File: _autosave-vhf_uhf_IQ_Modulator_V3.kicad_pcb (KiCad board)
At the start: 2 copper layers, 71 parts, among them J1 CONN_01X03, J2 TEST_1P, J3 Audio-Jack-3, J4 CONN_01X04, J5 SMA Edge FM, Q1 BC817-40, Q2 BC817-40, Q3 BC817-40, U1 TRF3701, U2 MMZ09332BT1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

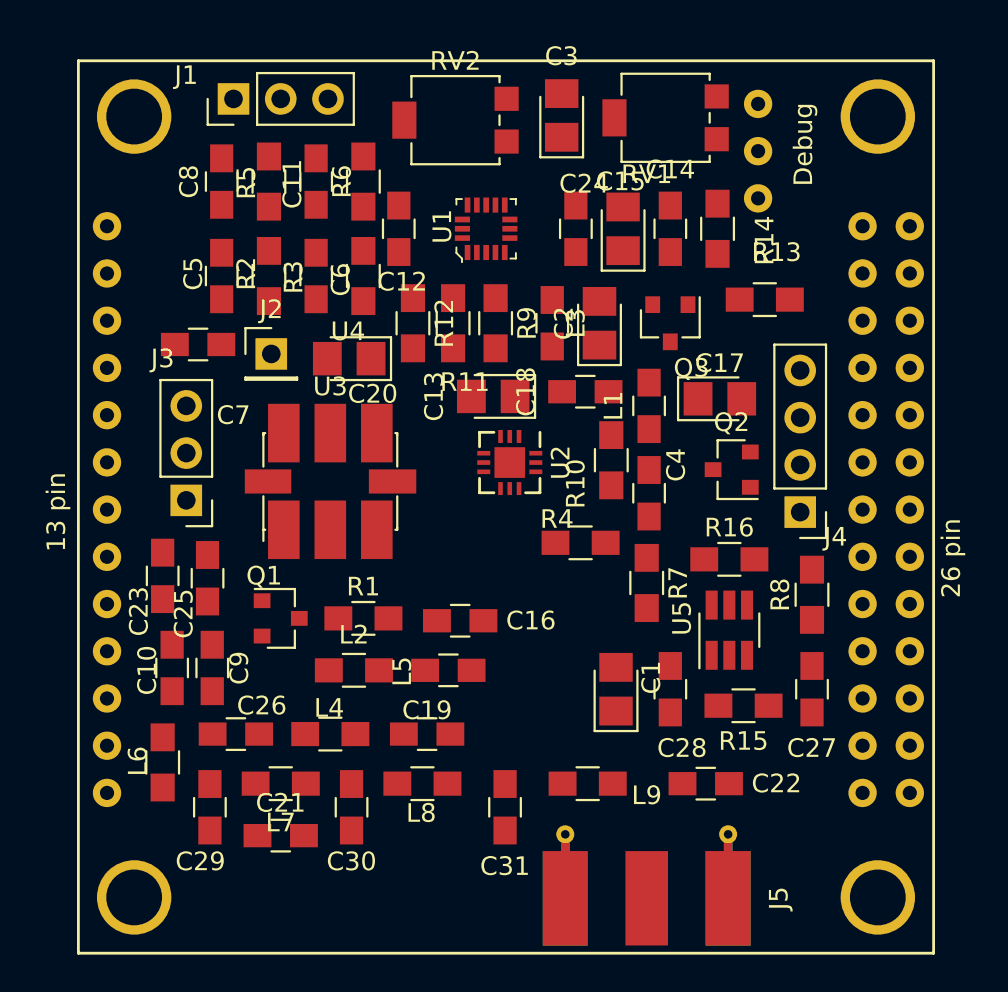
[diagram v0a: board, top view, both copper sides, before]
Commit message: fix lib and added Resistor
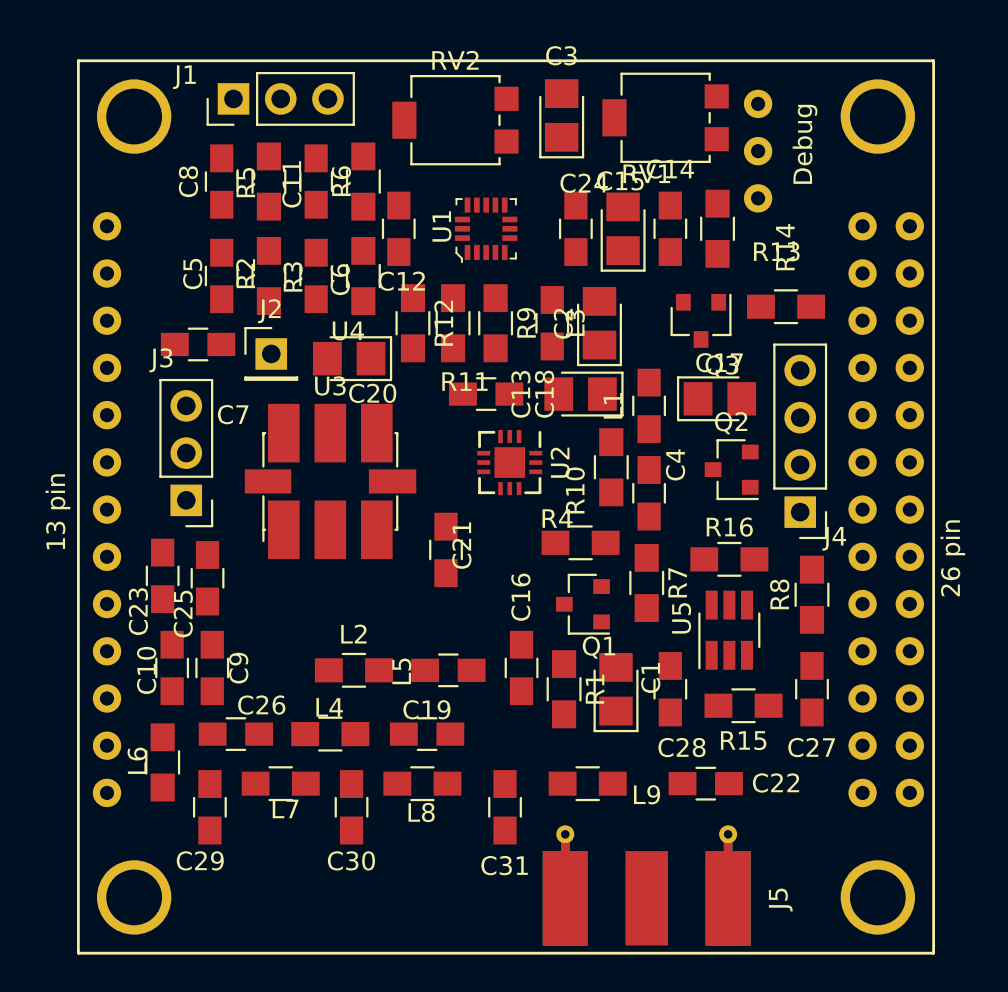
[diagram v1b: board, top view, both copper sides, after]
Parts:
- moved C21 17.8 mm to (168.3, 83.3), turned to 90 degrees
- moved Q1 16.3 mm to (175.6, 86.2), turned to 180 degrees
- moved R1 11.4 mm to (174.6, 90.8), turned to 270 degrees
- moved C18 5.34 mm to (170.4, 74.9), turned to 0 degrees
- moved C13 4.70 mm to (175.5, 74.9)
- moved C16 4.17 mm to (172.3, 89.7), turned to 270 degrees
- moved Q3 1.66 mm to (182.0, 71.0)
- moved R14 1.20 mm to (186.6, 70.2)
- moved R10 0.38 mm to (177.2, 78.9)
